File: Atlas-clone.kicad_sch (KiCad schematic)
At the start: 10 parts, among them J1 Conn_01x01, J2 Conn_01x01, J3 Conn_01x01, J4 Conn_01x32, J5 Conn_01x32, J6 Conn_01x16, J7 Conn_01x16

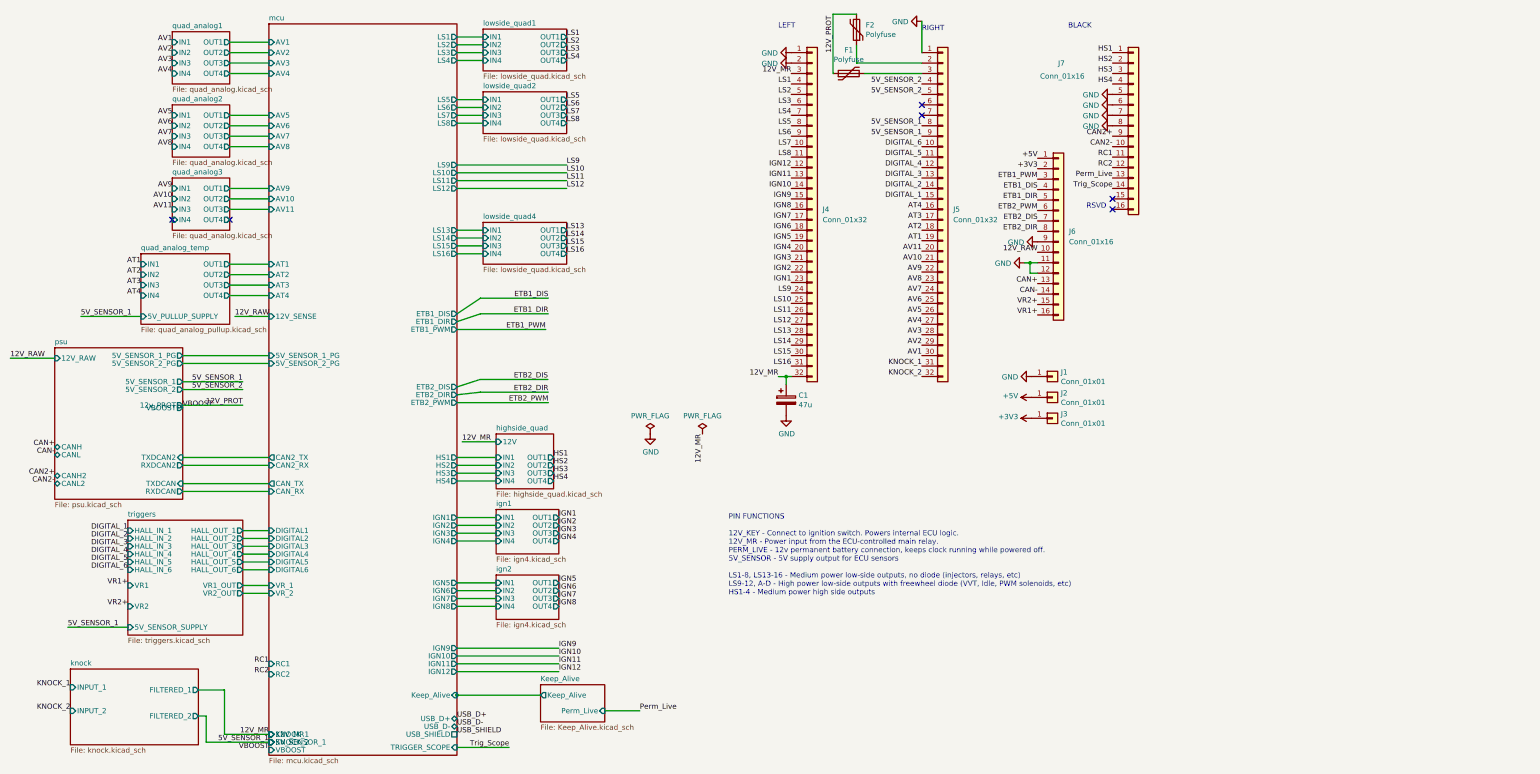
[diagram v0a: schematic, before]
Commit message: fome-mc: implement integrated motorcycle ECU schematics, 474-part PCB, BOM/CPL, DESIGN.md, and VALIDATION.md
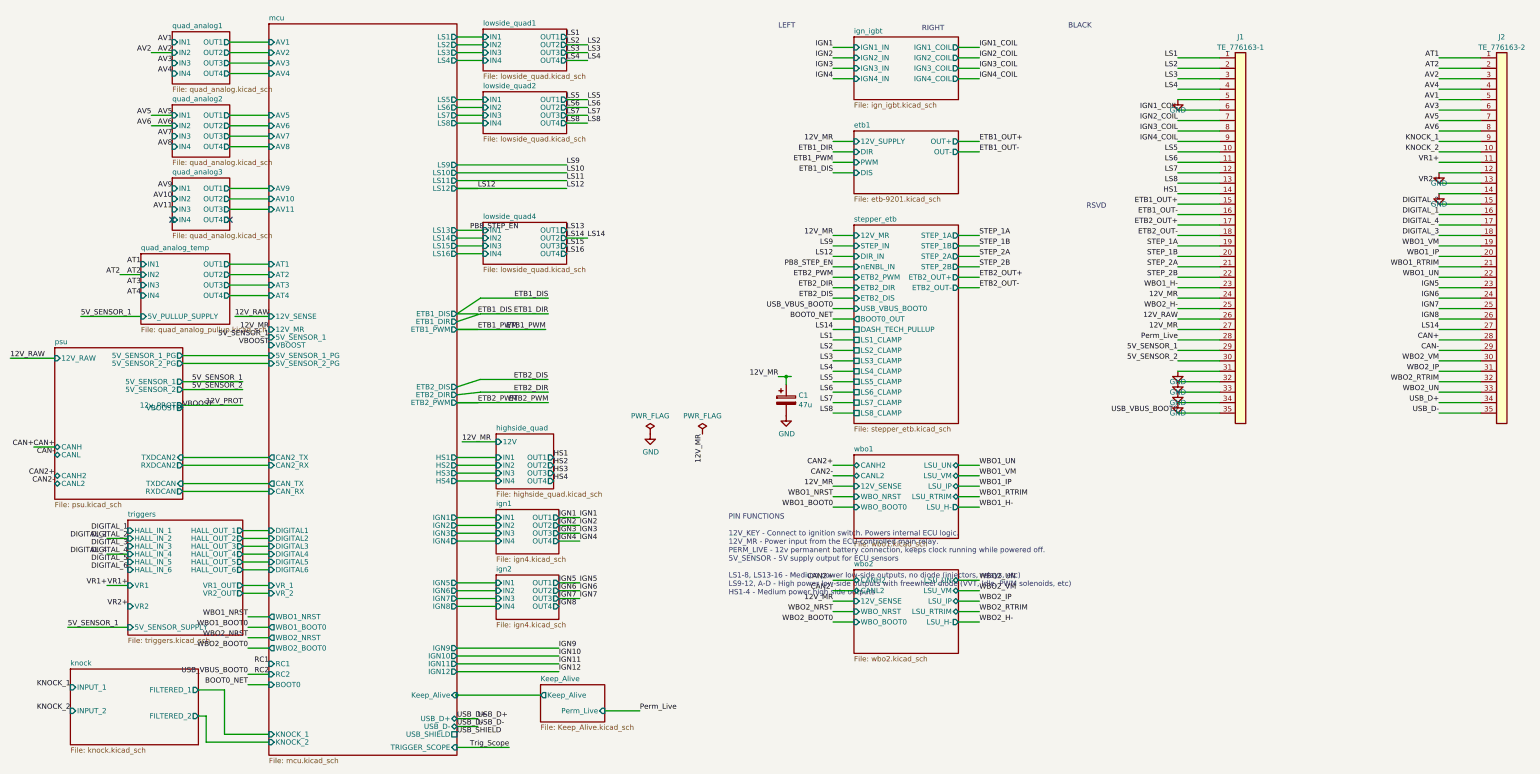
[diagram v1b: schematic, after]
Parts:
- removed F1, F2: Polyfuse, Resistor_SMD:R_1206_3216Metric, symbol Device:Polyfuse
- removed J1, J2, J3: Conn_01x01, TestPoint:TestPoint_Pad_D3.0mm, symbol Connector_Generic:Conn_01x01
- removed J4, J5: Conn_01x32, Connector_PinHeader_2.54mm:PinHeader_1x32_P2.54mm_Vertical, symbol Connector_Generic:Conn_01x32
- removed J6, J7: Conn_01x16, Connector_PinHeader_2.54mm:PinHeader_1x16_P2.54mm_Vertical, symbol Connector_Generic:Conn_01x16
- added J1: TE_776163-1, ampseal:ampseal-35, symbol Connector_Generic:Conn_01x35
- added J2: TE_776163-2, ampseal:ampseal-35-2, symbol Connector_Generic:Conn_01x35
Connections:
- net 12V_MR: now also J1.24 (Pin_24), J1.27 (Pin_27)
- net 12V_RAW: now also J1.26 (Pin_26)
- net 5V_SENSOR_1: now also J1.29 (Pin_29)
- net 5V_SENSOR_2: now also J1.30 (Pin_30)
- net AT1: now also J2.1 (Pin_1)
- net AT2: now also J2.2 (Pin_2)
- net AV1: now also J2.5 (Pin_5)
- net AV2: now also J2.3 (Pin_3)
- net AV3: now also J2.6 (Pin_6)
- net AV4: now also J2.4 (Pin_4)
- net AV5: now also J2.7 (Pin_7)
- net AV6: now also J2.8 (Pin_8)
- net CAN+: now also J2.28 (Pin_28)
- net CAN-: now also J2.29 (Pin_29)
- net DIGITAL_1: now also J2.16 (Pin_16)
- net DIGITAL_2: now also J2.15 (Pin_15)
- net DIGITAL_3: now also J2.18 (Pin_18)
- net DIGITAL_4: now also J2.17 (Pin_17)
- net GND: now also J1.31 (Pin_31), J1.32 (Pin_32), J1.33 (Pin_33), J1.34 (Pin_34), J1.5 (Pin_5), J2.12 (Pin_12), J2.14 (Pin_14)
- net HS1: now also J1.14 (Pin_14)
- net IGN5: now also J2.23 (Pin_23)
- net IGN6: now also J2.24 (Pin_24)
- net IGN7: now also J2.25 (Pin_25)
- net IGN8: now also J2.26 (Pin_26)
- net KNOCK_1: now also J2.9 (Pin_9)
- net KNOCK_2: now also J2.10 (Pin_10)
- net LS1: now also J1.1 (Pin_1)
- net LS14: now also J2.27 (Pin_27)
- net LS2: now also J1.2 (Pin_2)
- net LS3: now also J1.3 (Pin_3)
- net LS4: now also J1.4 (Pin_4)
- net LS5: now also J1.10 (Pin_10)
- net LS6: now also J1.11 (Pin_11)
- net LS7: now also J1.12 (Pin_12)
- net LS8: now also J1.13 (Pin_13)
- net Perm_Live: now also J1.28 (Pin_28)
- net RC2: now also J1.35 (Pin_35)
- net USB_D+: now also J2.34 (Pin_34)
- net USB_D-: now also J2.35 (Pin_35)
- net VR1+: now also J2.11 (Pin_11)
- net VR2+: now also J2.13 (Pin_13)
- new net ETB1_OUT+: J1.15 (Pin_15)
- new net ETB1_OUT-: J1.16 (Pin_16)
- new net ETB2_OUT+: J1.17 (Pin_17)
- new net ETB2_OUT-: J1.18 (Pin_18)
- new net IGN1_COIL: J1.6 (Pin_6)
- new net IGN2_COIL: J1.7 (Pin_7)
- new net IGN3_COIL: J1.8 (Pin_8)
- new net IGN4_COIL: J1.9 (Pin_9)
- new net STEP_1A: J1.19 (Pin_19)
- new net STEP_1B: J1.20 (Pin_20)
- new net STEP_2A: J1.21 (Pin_21)
- new net STEP_2B: J1.22 (Pin_22)
- new net WBO1_H-: J1.23 (Pin_23)
- new net WBO1_IP: J2.20 (Pin_20)
- new net WBO1_RTRIM: J2.21 (Pin_21)
- new net WBO1_UN: J2.22 (Pin_22)
- new net WBO1_VM: J2.19 (Pin_19)
- new net WBO2_H-: J1.25 (Pin_25)
- new net WBO2_IP: J2.31 (Pin_31)
- new net WBO2_RTRIM: J2.32 (Pin_32)
- new net WBO2_UN: J2.33 (Pin_33)
- new net WBO2_VM: J2.30 (Pin_30)
- no-connect marks 6 -> 2
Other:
- added sheet etb1 (etb-9201.kicad_sch)
- added sheet ign_igbt (ign_igbt.kicad_sch)
- added sheet stepper_etb (stepper_etb.kicad_sch)
- added sheet wbo1 (wbo1.kicad_sch)
- added sheet wbo2 (wbo2.kicad_sch)
- sheet mcu ports: added BOOT0, WBO1_BOOT0, WBO1_NRST, WBO2_BOOT0, WBO2_NRST; removed none
- title: Atlas-clone -> fome-mc Integrated Motorcycle ECU
